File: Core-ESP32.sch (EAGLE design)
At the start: 68 parts, among them J3 CONNECTOR-GROVE-4P-2.0-347013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, Q1 BSS138, Q10 BSS138, Q11 BSS138, Q12 BSS138, Q13 BSS138, Q14 BSS138, Q2 BSS138, Q3 BSS138, Q4 BSS138, Q5 BSS138, Q6 BSS138, Q7 BSS138, Q8 BSS138, Q9 BSS138

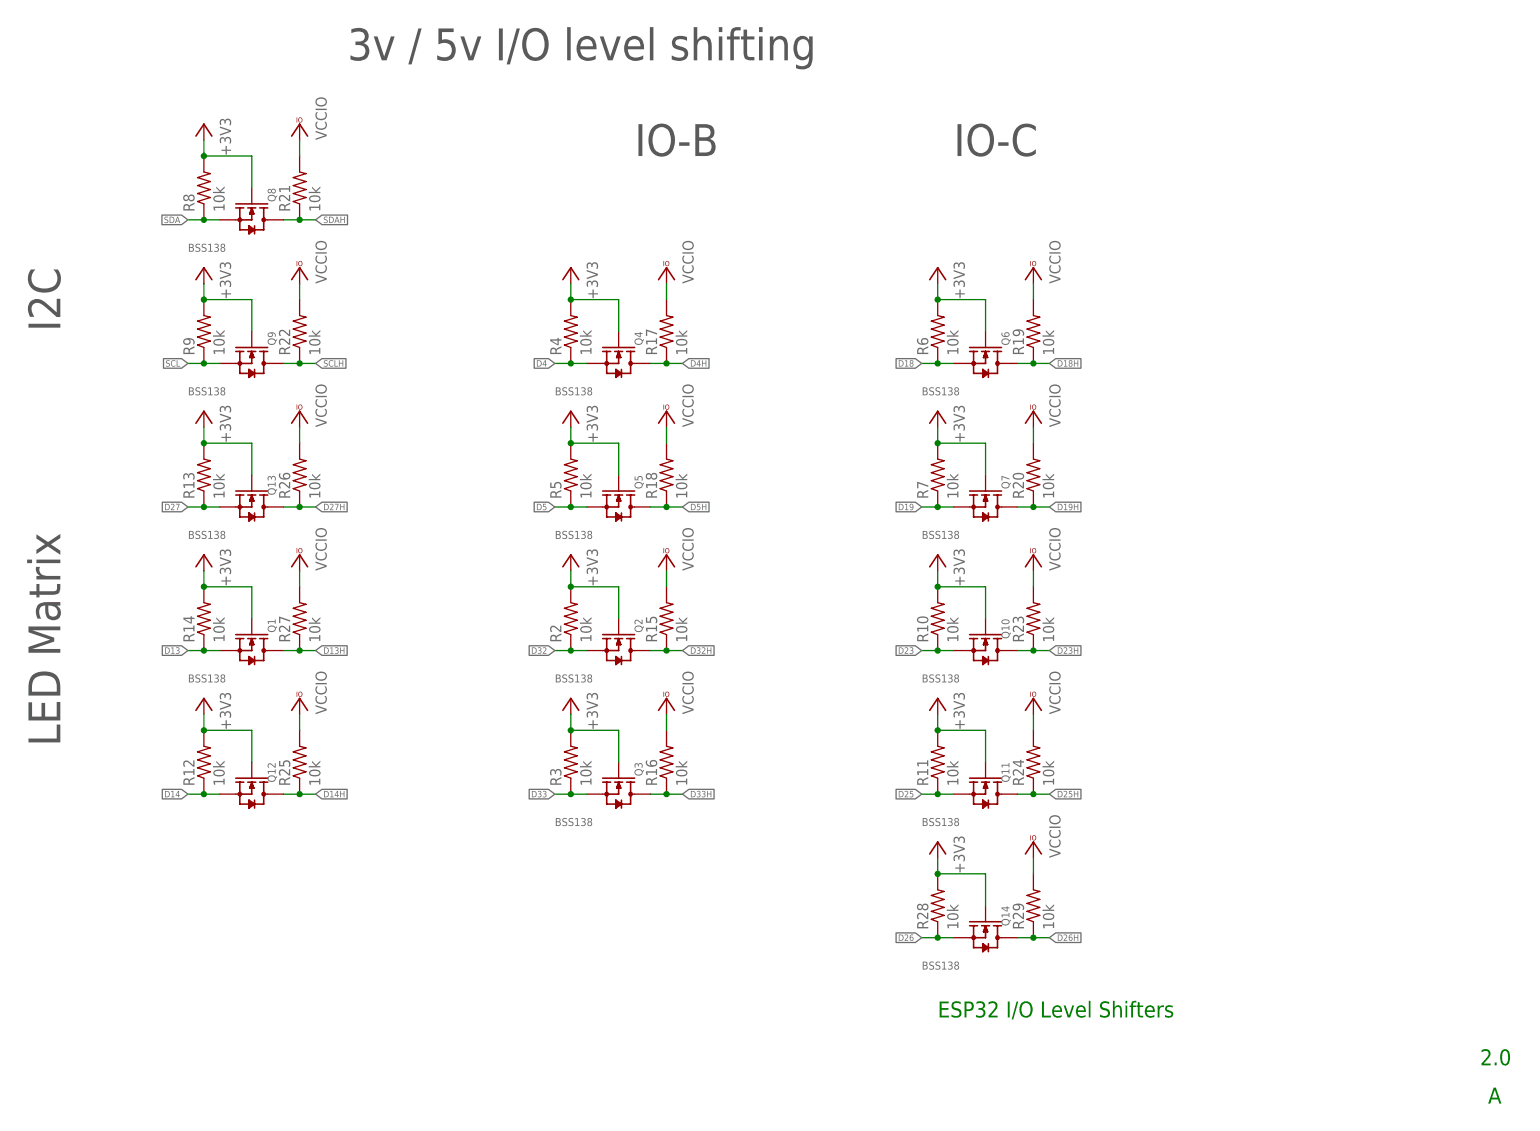
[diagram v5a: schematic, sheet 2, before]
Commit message: switched to 30-pin dev board from larger Geekreit one
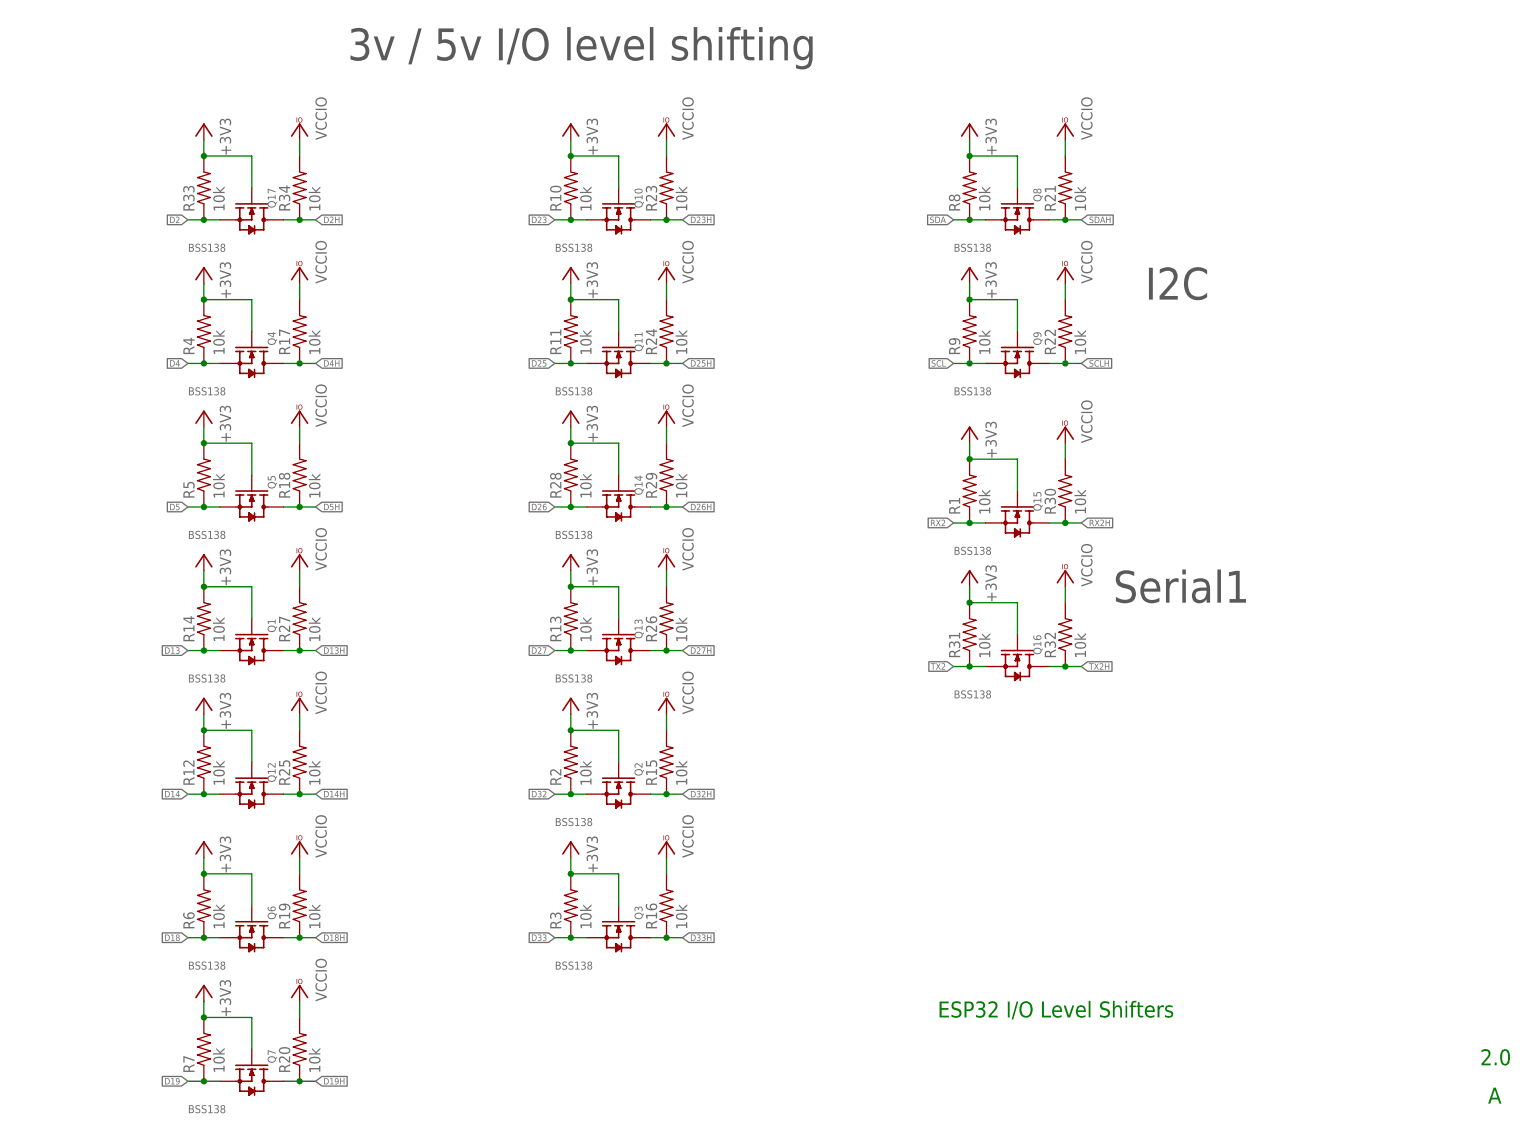
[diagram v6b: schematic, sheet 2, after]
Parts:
- removed IO-A: (no value), SparkFun-Connectors:M06LOCK
- removed J1: (no value), SPCoast:CONNECTOR-RJ25-43860-2-MOLEX
- removed MT1, MT2, MT3, MT4: MOUNTINGHOLE, SPCoast:MOUNTINGHOLE
- added CON1: (no value), SPCoast:CONNECTOR-M05LOCK
- added FID1, FID2: FIDUCIAL, SPCoast:FIDUCIAL
- added Q15, Q16, Q17: BSS138, SPCoast:MOSFET-N-BSS138-SOT23
- added R1, R30, R31, R32, R33, R34: 10k, SPCoast:R0603-RES
- BOARD: device SPCoast:BOARD80X100-NOHOLES -> SPCoast:BOARD80X100-IOB
- IO-B, IO-C, IO-D: device SparkFun-Connectors:M06LOCK -> SPCoast:CONNECTOR-M06LOCK
- LABEL1: device SPCoast-minimal:POWER_LABEL -> SPCoast:DOC-POWER_LABEL
- U$1: value ESP32-GEEKCREITDOITV1 -> ESP32/DEV; device SPCoast:ESP32-GEEKCREITDOITV1 -> SPCoast:ESP32/DEV
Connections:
- removed net D0: U$1.GPIO0
- new net D2H: CON1.1, Q17.D, R34.1
- new net RX2H: CON1.2, Q15.D, R30.1
- new net TX2H: CON1.3, Q16.D, R32.1
- net +3V3: now also Q15.G, Q16.G, Q17.G, R1.2, R31.2, R33.2; no longer IO-A.1, J1.1
- net D2: now also Q17.S, R33.1
- net GND: now also CON1.5; no longer IO-A.6, J1.6
- net RX: no longer IO-A.3, J1.3
- net RX2: now also Q15.S, R1.1; no longer IO-A.5, J1.5
- net TX: no longer IO-A.2, J1.2
- net TX2: now also Q16.S, R31.1; no longer IO-A.4, J1.4
- net VCCIO: now also CON1.4, R30.2, R32.2, R34.2
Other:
- note added: "5V"
- note added: "5V Safe"
- note added: "CMRI"
- note added: "GND"
- note added: "IO & I2C Adapter for ESP32-DEV"
- note added: "Processor carrier board for ESP32-DEV Breaks out 5v I2C, IO4 style headers and Matrix Display"
- note added: "RXDATA/CMRI"
- note added: "Serial1"
- note added: "TXDATA/CMRI"
- note added: "TXEN/CMRI"
- note removed: "Codeline Matrix"
- note removed: "IO & I2C Adapter for Geekcreit ESP32"
- note removed: "IO-B"
- note removed: "IO-C"
- note removed: "Processor carrier board for Geekcreit ESP32 Breaks out 5v I2C, IO4 style headers and Matrix Display 2.1->2.2: change from 0805 to 0603 footprints 2.4: codeline is now I2C, add more I/Os"
- moved on the sheet: Q10, Q11, Q13, Q14, Q2, Q3, Q4, Q5, Q6, Q7, Q8, Q9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

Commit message: cleanup
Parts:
- removed I2CLED1: (no value), SPCoast:CONNECTOR-M04LOCK
- removed J3: CONNECTOR-GROVE-4P-2.0-3470130P1, SPCoast:CONNECTOR-GROVE-4P-2.0-3470130P1
- added LED1: G, SPCoast:LED0603-LED
- added PWROUT: CONNECTOR-POWER-R, SPCoast:CONNECTOR-POWER-R
- added R35: 2k2, SPCoast:R0603-RES
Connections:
- new net N$1: LED1.A, R35.1
- net +3V3: no longer I2CLED1.3
- net +9V: now also PWROUT.V+; no longer J3.3, J3.4
- net GND: now also LED1.C, PWROUT.GND; no longer I2CLED1.4, J3.1, J3.2
- net SCL: no longer I2CLED1.2
- net SDA: no longer I2CLED1.1
- net VCCIO: now also R35.2
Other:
- note added: "3.0"
- note added: "3v3 only"
- note added: "ESP32-DEV WROOM32"
- note added: "Processor carrier board for ESP32-DEV Breaks out 5v I2C, IO4 style headers and I2C OLED Display"
- note added: "SSD 1306 OLED display"
- note removed: "2.4"
- note removed: "Geekcreit/DOIT ESP32"
- note removed: "LED"
- note removed: "LED Matrix"
- note removed: "Processor carrier board for ESP32-DEV Breaks out 5v I2C, IO4 style headers and Matrix Display"
- moved on the sheet: C1, C2, C3, CON1, I2C, I2CLED32, I2CLED64, IO-B, IO-C, IO-D, J2, J4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

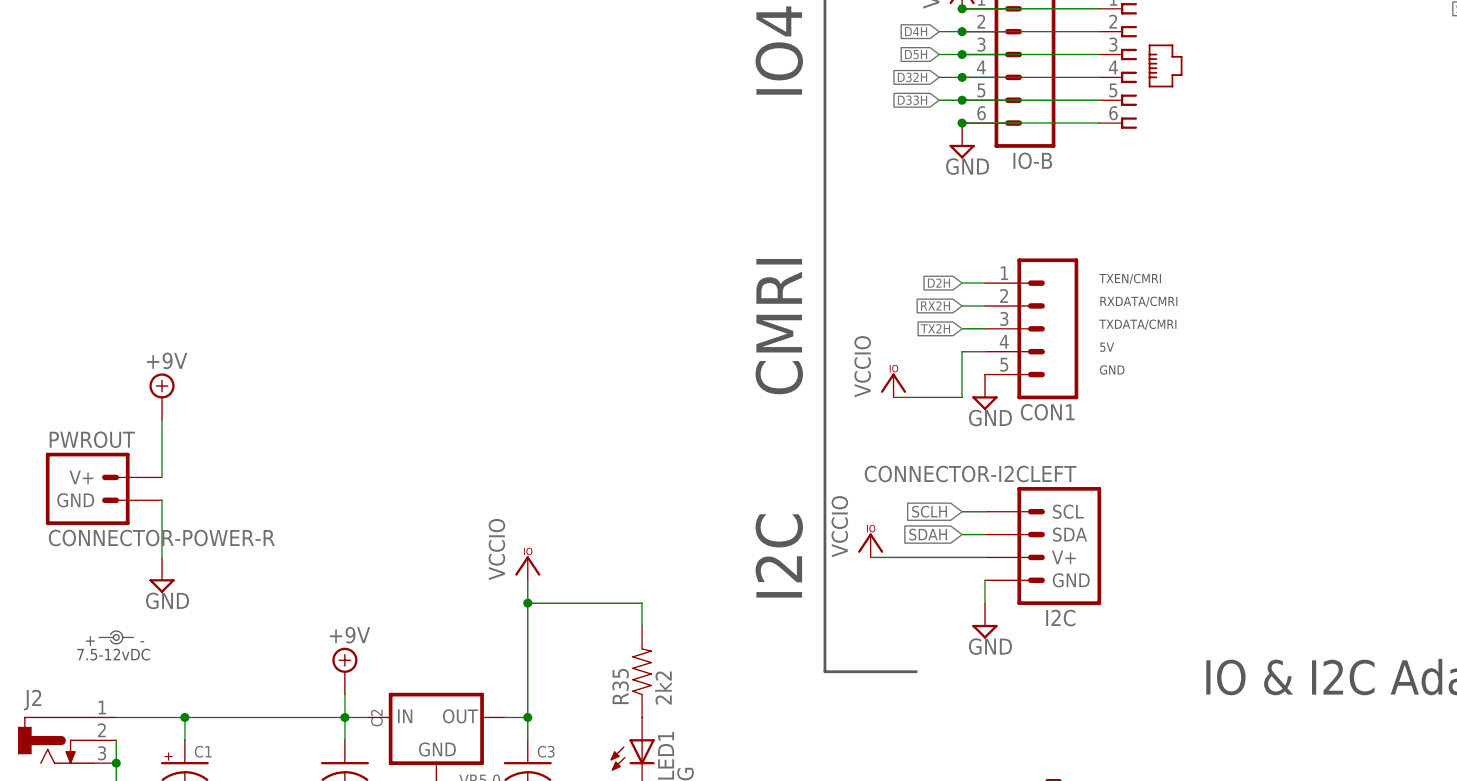
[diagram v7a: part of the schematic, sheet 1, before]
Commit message: convert to 30-pin DEV board, add CMRI-net IO
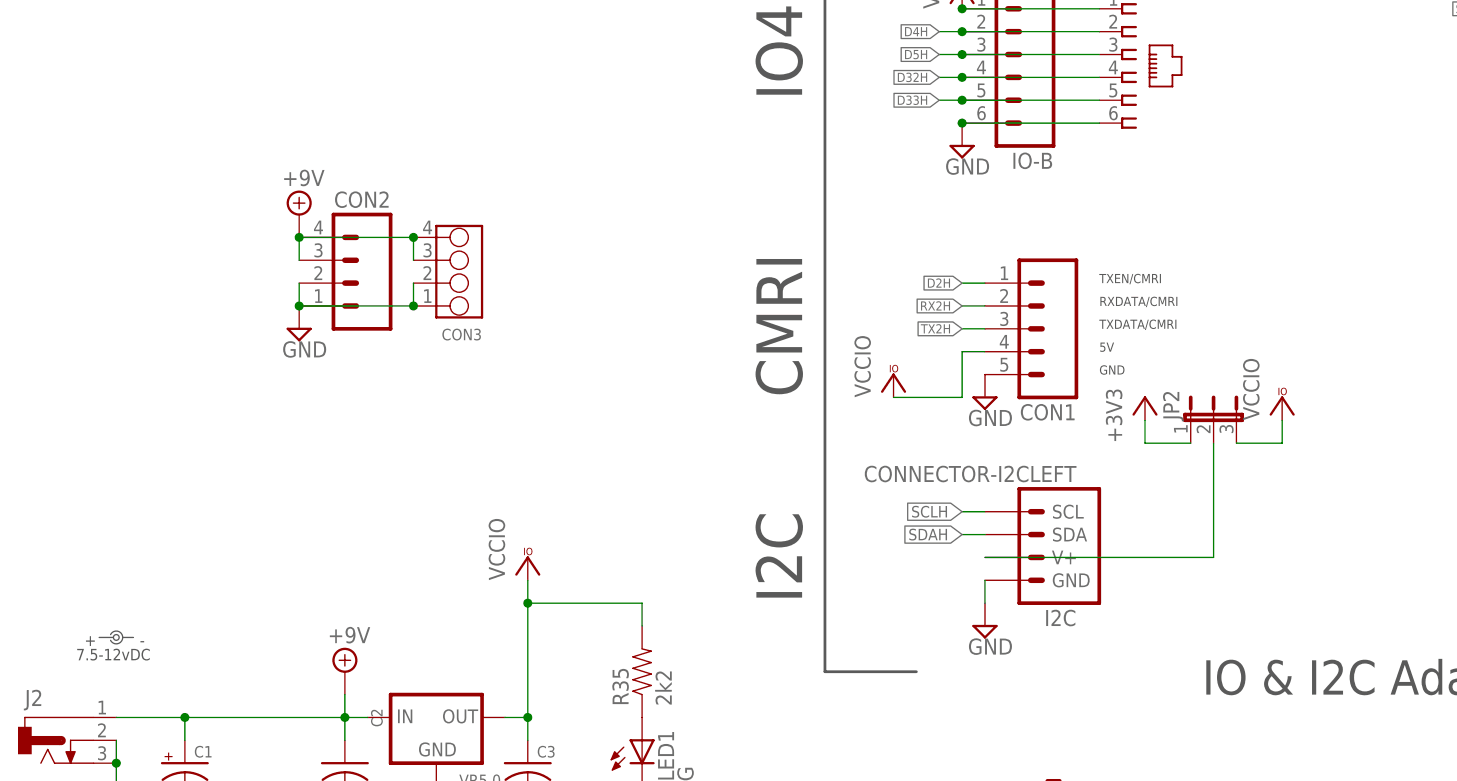
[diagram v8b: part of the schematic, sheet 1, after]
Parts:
- removed PWROUT: CONNECTOR-POWER-R, SPCoast:CONNECTOR-POWER-R
- added CON2: (no value), SPCoast:CONNECTOR-M04LOCK
- added CON3: (no value), SPCoast:CONNECTOR-GROVE-4P-2.0-3470130P1
- added JP2: (no value), SPCoast:JUMPER-3PTH-LOCK
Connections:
- new net N$3: I2C.V+, JP2.2
- net +3V3: now also JP2.1
- net +9V: now also CON2.3, CON2.4, CON3.3, CON3.4; no longer PWROUT.V+
- net GND: now also CON2.1, CON2.2, CON3.1, CON3.2; no longer PWROUT.GND
- net VCCIO: now also JP2.3; no longer I2C.V+
